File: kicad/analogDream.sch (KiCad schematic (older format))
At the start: 69 parts, among them K1 RefJump, P1 CONN_4X2, P2 CONN_4X2, P3 CONN_7X2, P4 CONN_7X2, P5 CONN_4X2, P6 CONN_4X2, U1 AD8221, U10 LT1026, U2 TL072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

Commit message: modified schematic to work off 2.5v reference
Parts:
- removed C1, C2, C7: 220n, symbol C
- removed C3, C4, C5, C6: 10u, symbol CP1
- removed K1: RefJump, symbol CONN_3
- removed P1, P5: CONN_4X2, symbol CONN_4X2
- removed P3: CONN_7X2, symbol CONN_7X2
- removed PC2: Ch2, symbol CONN_2
- removed PC5: 5V_GND, symbol CONN_2
- removed PC6: out_1_2, symbol CONN_2
- removed PC8: AREF_GND, symbol CONN_2
- removed PC9: +V_-V, symbol CONN_2
- removed R1: 47k, symbol R
- removed R10, R11, R17, R18: 10k, symbol R
- removed R2, R23, R27, R9: 18k, symbol R
- removed R21, R7: 182, symbol R
- removed R22, R8: 2k, symbol R
- removed R28: 49.9k, symbol R
- removed R29: 12.4k, symbol R
- removed R30: 5.49k, symbol R
- removed R31: 1k, symbol R
- removed R32: 499, symbol R
- removed R33: 100, symbol R
- removed R5: 12k, symbol R
- removed RV1, RV3: 10k, symbol POT
- removed U10: LT1026, symbol LT1026
- removed U3: AD8221, symbol AD8221
- removed unit 2 of U4
- added R? (x2): 10k, symbol R
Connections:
- net labels added: 2.5v
- net labels removed: +12V, -12V, AREF, in_ch2+, in_ch2-, out_ch2
- wire segments 154 -> 68
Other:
- moved on the sheet: PC1, U4A

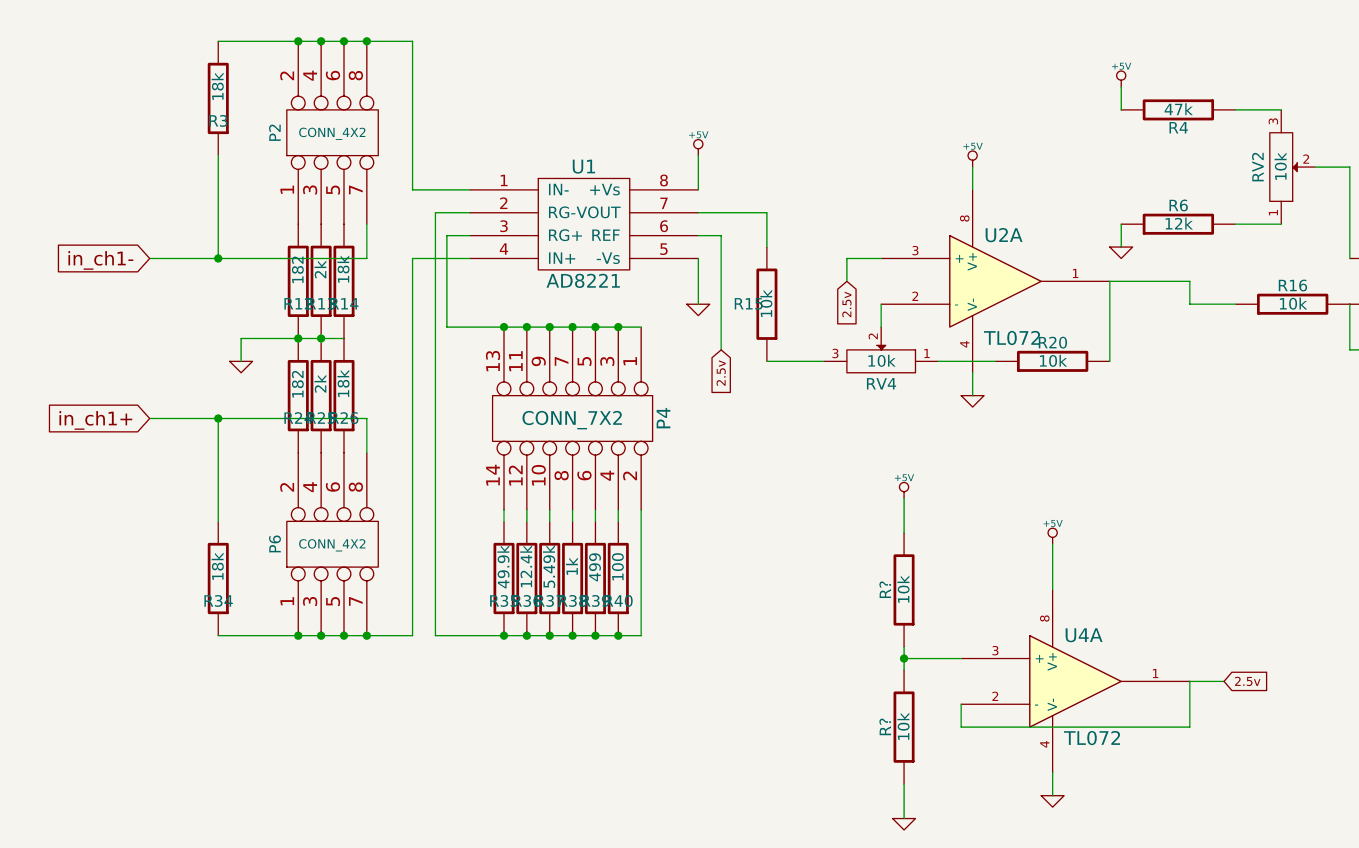
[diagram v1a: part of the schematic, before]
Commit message: Changed resitor values, added caps
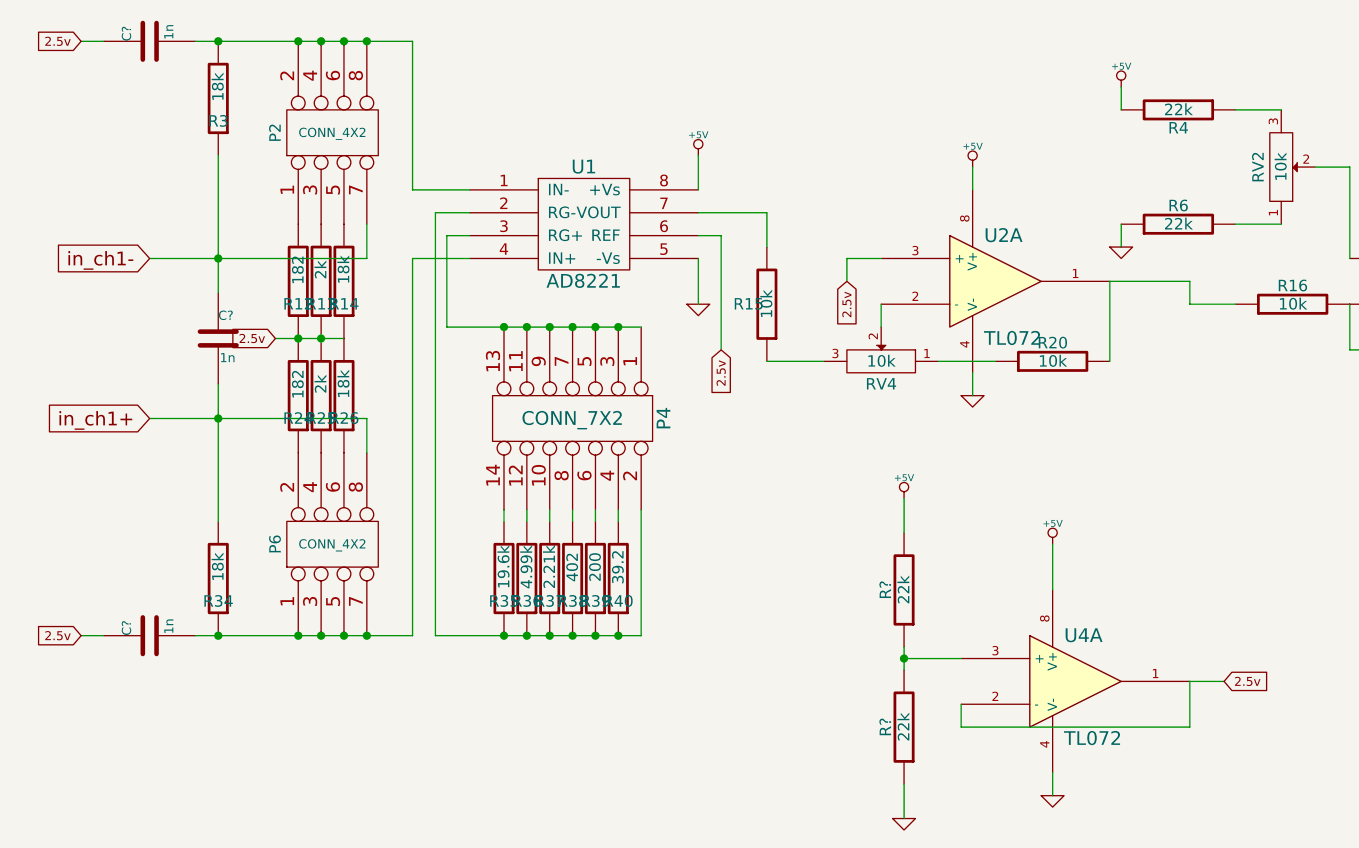
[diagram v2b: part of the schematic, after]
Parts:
- added C? (x3): 1n, ~, symbol C
- R35: value 49.9k -> 19.6k
- R36: value 12.4k -> 4.99k
- R37: value 5.49k -> 2.21k
- R38: value 1k -> 402
- R39: value 499 -> 200
- R4: value 47k -> 22k
- R40: value 100 -> 39.2
- R6: value 12k -> 22k
- R? (x2): value 10k -> 22k
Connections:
- net 2.5v: now also R12.1, R13.1, R14.1, R24.2, R25.2, R26.2, C?.1, C?.1
- net GND: no longer R12.1, R13.1, R14.1, R24.2, R25.2, R26.2
- net in_ch1+: now also C?.2
- net in_ch1-: now also C?.1
- net at P2.2, P2.4, P2.6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: now also C?.2
- net at P6.1, P6.3, P6.5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: now also C?.2
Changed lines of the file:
@@
 Sheet 1 1
 Title "Analog Dream Board Shield"
-Date "20 jul 2013"
+Date "4 aug 2013"
 Rev ""
 Comp "Visgence Technologies"
@@
 	1050 1650 2000 1650
 Wire Wire Line
-	1350 3300 2200 3300
-Wire Wire Line
-	2200 1350 2200 700
+	1250 3300 2200 3300
+Wire Wire Line
+	2200 700  2200 1350
 Wire Wire Line
 	2200 1350 2450 1350
@@
 	2200 1650 2450 1650
 Wire Wire Line
-	1350 2350 1350 2800
+	1350 2200 1350 2800
 Wire Wire Line
 	2000 2500 2000 2350
@@
 Connection ~ 2800 3300
 Connection ~ 3000 3300
-Wire Wire Line
-	1900 2000 1450 2000
-Wire Wire Line
-	1450 2000 1450 2100
 Connection ~ 1700 2000
 Connection ~ 1900 3300
@@
 Connection ~ 1700 700
 Wire Wire Line
-	1350 1650 1350 1200
-Wire Wire Line
-	2200 700  1350 700
+	1350 1200 1350 1800
+Wire Wire Line
+	1250 700  2200 700
 Wire Wire Line
 	2000 2350 1050 2350
@@
 $EndComp
 $Comp
-L GND #PWR022
-U 1 1 4ED2A54E
-P 1450 2100
-F 0 "#PWR022" H 1450 2100 30  0001 C CNN
-F 1 "GND" H 1450 2030 30  0001 C CNN
-F 2 "" H 1450 2100 60  0001 C CNN
-F 3 "" H 1450 2100 60  0001 C CNN
-	1    1450 2100
-	1    0    0    -1
-$EndComp
-$Comp
 L R R12
 U 1 1 4ED2A4F1
@@
 P 3100 3050
 F 0 "R40" H 3100 3150 50  0000 C CNN
-F 1 "100" V 3100 3000 50  0000 C CNN
+F 1 "39.2" V 3100 3000 50  0000 C CNN
 F 2 "" H 3100 3050 60  0001 C CNN
 F 3 "" H 3100 3050 60  0001 C CNN
@@
 P 3000 3050
 F 0 "R39" H 3000 3150 50  0000 C CNN
-F 1 "499" V 3000 3000 50  0000 C CNN
+F 1 "200" V 3000 3000 50  0000 C CNN
 F 2 "" H 3000 3050 60  0001 C CNN
 F 3 "" H 3000 3050 60  0001 C CNN
@@
 P 2900 3050
 F 0 "R38" H 2900 3150 50  0000 C CNN
-F 1 "1k" V 2900 3000 50  0000 C CNN
+F 1 "402" V 2900 3000 50  0000 C CNN
 F 2 "" H 2900 3050 60  0001 C CNN
 F 3 "" H 2900 3050 60  0001 C CNN
@@
 P 2800 3050
 F 0 "R37" H 2800 3150 50  0000 C CNN
-F 1 "5.49k" V 2800 3000 50  0000 C CNN
+F 1 "2.21k" V 2800 3000 50  0000 C CNN
 F 2 "" H 2800 3050 60  0001 C CNN
 F 3 "" H 2800 3050 60  0001 C CNN
@@
 P 2700 3050
 F 0 "R36" H 2700 3150 50  0000 C CNN
-F 1 "12.4k" V 2700 3000 50  0000 C CNN
+F 1 "4.99k" V 2700 3000 50  0000 C CNN
 F 2 "" H 2700 3050 60  0001 C CNN
 F 3 "" H 2700 3050 60  0001 C CNN
@@
 P 2600 3050
 F 0 "R35" H 2600 3150 50  0000 C CNN
-F 1 "49.9k" V 2600 3000 50  0000 C CNN
+F 1 "19.6k" V 2600 3000 50  0000 C CNN
 F 2 "" H 2600 3050 60  0001 C CNN
 F 3 "" H 2600 3050 60  0001 C CNN
@@
 P 5550 1000
 F 0 "R4" V 5630 1000 50  0000 C CNN
-F 1 "47k" V 5550 1000 50  0000 C CNN
+F 1 "22k" V 5550 1000 50  0000 C CNN
 F 2 "" H 5550 1000 60  0001 C CNN
 F 3 "" H 5550 1000 60  0001 C CNN
@@
 P 5550 1500
 F 0 "R6" V 5630 1500 50  0000 C CNN
-F 1 "12k" V 5550 1500 50  0000 C CNN
+F 1 "22k" V 5550 1500 50  0000 C CNN
 F 2 "" H 5550 1500 60  0001 C CNN
 F 3 "" H 5550 1500 60  0001 C CNN
@@
 P 4350 3100
 F 0 "R?" V 4430 3100 50  0000 C CNN
-F 1 "10k" V 4350 3100 50  0000 C CNN
+F 1 "22k" V 4350 3100 50  0000 C CNN
 F 2 "" H 4350 3100 60  0001 C CNN
 F 3 "" H 4350 3100 60  0001 C CNN
@@
 P 4350 3700
 F 0 "R?" V 4430 3700 50  0000 C CNN
-F 1 "10k" V 4350 3700 50  0000 C CNN
+F 1 "22k" V 4350 3700 50  0000 C CNN
 F 2 "" H 4350 3700 60  0001 C CNN
 F 3 "" H 4350 3700 60  0001 C CNN
@@
 Text GLabel 4100 1750 3    39   Input ~ 0
 2.5v
+Text GLabel 1600 2000 0    39   Input ~ 0
+2.5v
+Wire Wire Line
+	1600 2000 1900 2000
+$Comp
+L C C?
+U 1 1 51FEDA9D
+P 1350 2000
+F 0 "C?" H 1350 2100 40  0000 L CNN
+F 1 "1n" H 1356 1915 40  0000 L CNN
+F 2 "~" H 1388 1850 30  0000 C CNN
+F 3 "~" H 1350 2000 60  0000 C CNN
+	1    1350 2000
+	1    0    0    -1
+$EndComp
+$Comp
+L C C?
+U 1 1 51FEDB64
+P 1050 700
+F 0 "C?" H 1050 800 40  0000 L CNN
+F 1 "1n" H 1056 615 40  0000 L CNN
+F 2 "~" H 1088 550 30  0000 C CNN
+F 3 "~" H 1050 700 60  0000 C CNN
+	1    1050 700
+	0    -1   -1   0
+$EndComp
+$Comp
+L C C?
+U 1 1 51FEDB6A
+P 1050 3300
+F 0 "C?" H 1050 3400 40  0000 L CNN
+F 1 "1n" H 1056 3215 40  0000 L CNN
+F 2 "~" H 1088 3150 30  0000 C CNN
+F 3 "~" H 1050 3300 60  0000 C CNN
+	1    1050 3300
+	0    -1   -1   0
+$EndComp
+Connection ~ 1350 3300
+Connection ~ 1350 700
+Text GLabel 750  700  0    39   Input ~ 0
+2.5v
+Text GLabel 750  3300 0    39   Input ~ 0
+2.5v
+Wire Wire Line
+	750  3300 850  3300
+Wire Wire Line
+	750  700  850  700
 $EndSCHEMATC

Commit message: Added psu filter, changed opamp parts
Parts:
- removed U2, U4: TL072, symbol TL072
- added C4: 1n, ~, symbol C
- added C5: CP1, ~, symbol CP1
- added D1: LED, ~, symbol LED
- added R?: 2.2k, ~, symbol R
- added U2: TL074, symbol TL074
- C2: renamed from C?; value 1n -> 10n
- U1: value AD8221 -> AD8422
- gave numbers to parts that had none: 2
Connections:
- net +5V: now also C4.2, C5.1, R?.1, U2.4 (V+), U2.4 (V+), U2.4 (V+)
- net 2.5v: now also U2.3 (+), U2.8, U2.9 (-)
- net GND: now also C4.1, C5.2, D1.2 (K), U2.11 (V-), U2.11 (V-), U2.11 (V-)
- net out_ch1: now also U2.7
- net at RV4.2: now also U2.2 (-)
- net at R16.1, R20.2: now also U2.1
- net at R16.2, R19.1: now also U2.6 (-)
- net at RV2.2: now also U2.5 (+)
- net at R?.1, R?.2: now also U2.10 (+)
- new net: D1.1 (A), R?.2
